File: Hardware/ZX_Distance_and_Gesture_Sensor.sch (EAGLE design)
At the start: 27 parts, among them Q1 MMBT2222A, Q2 MOSFET-NCHANNEL2N7002PW

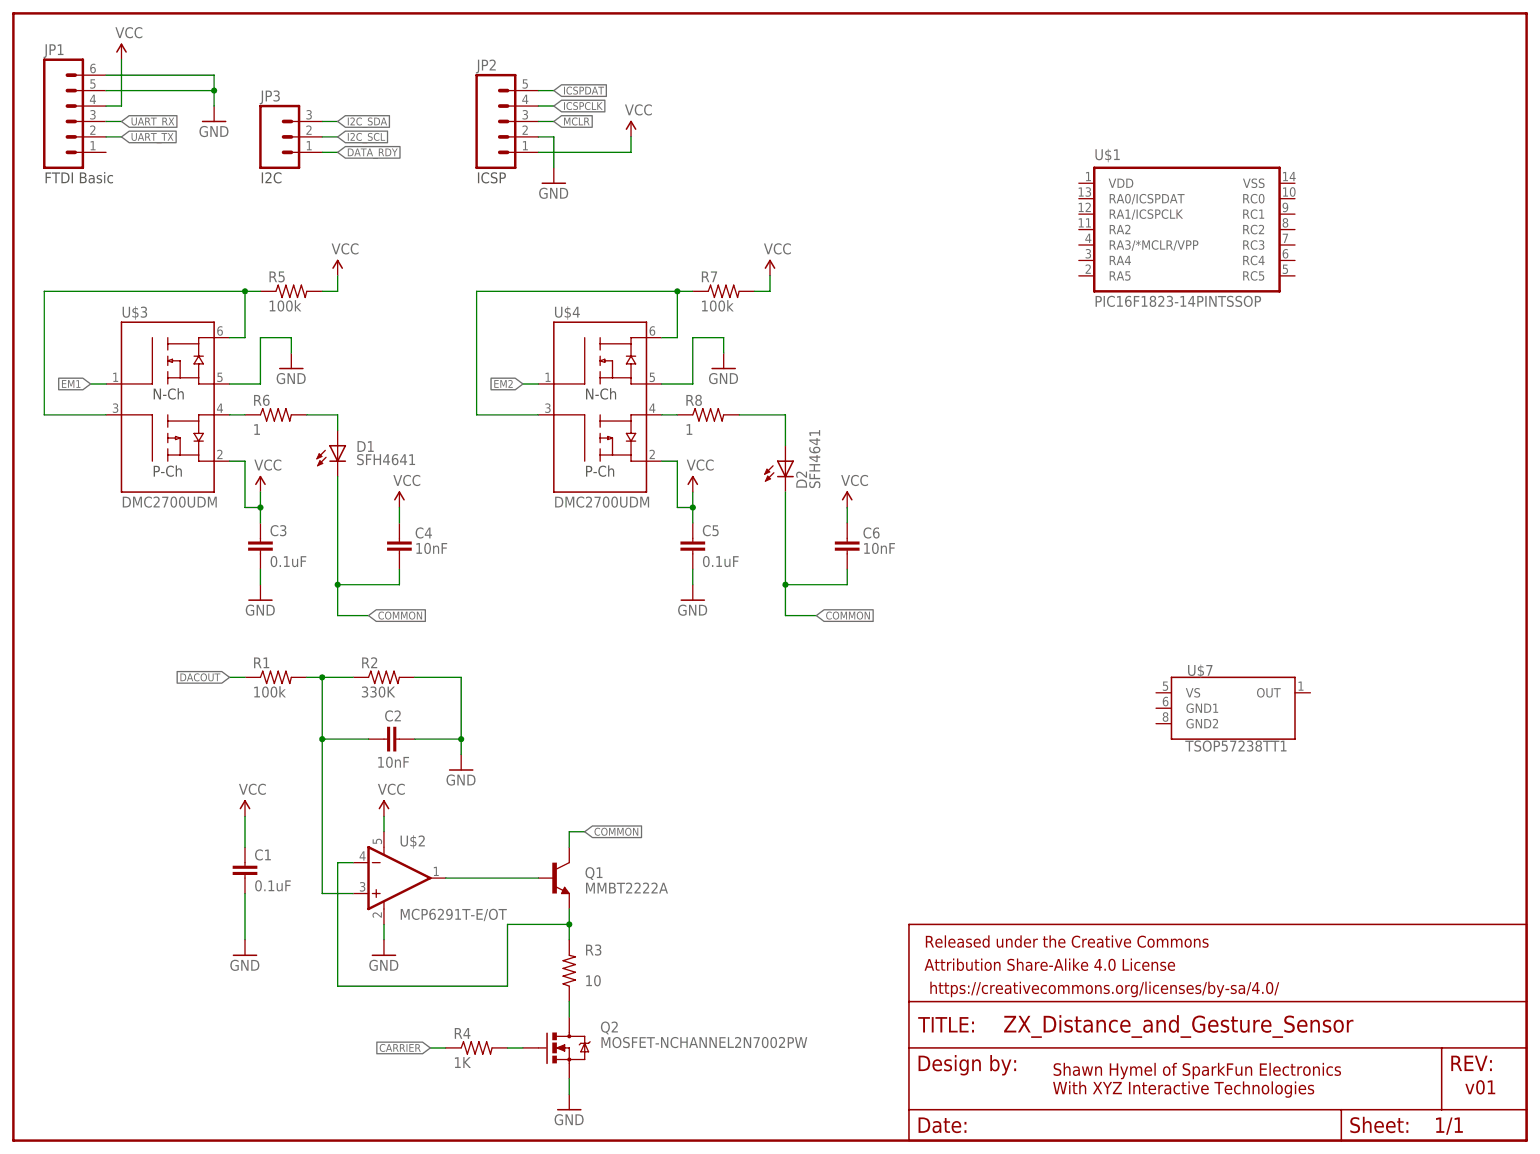
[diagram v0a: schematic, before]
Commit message: Created initial schematic
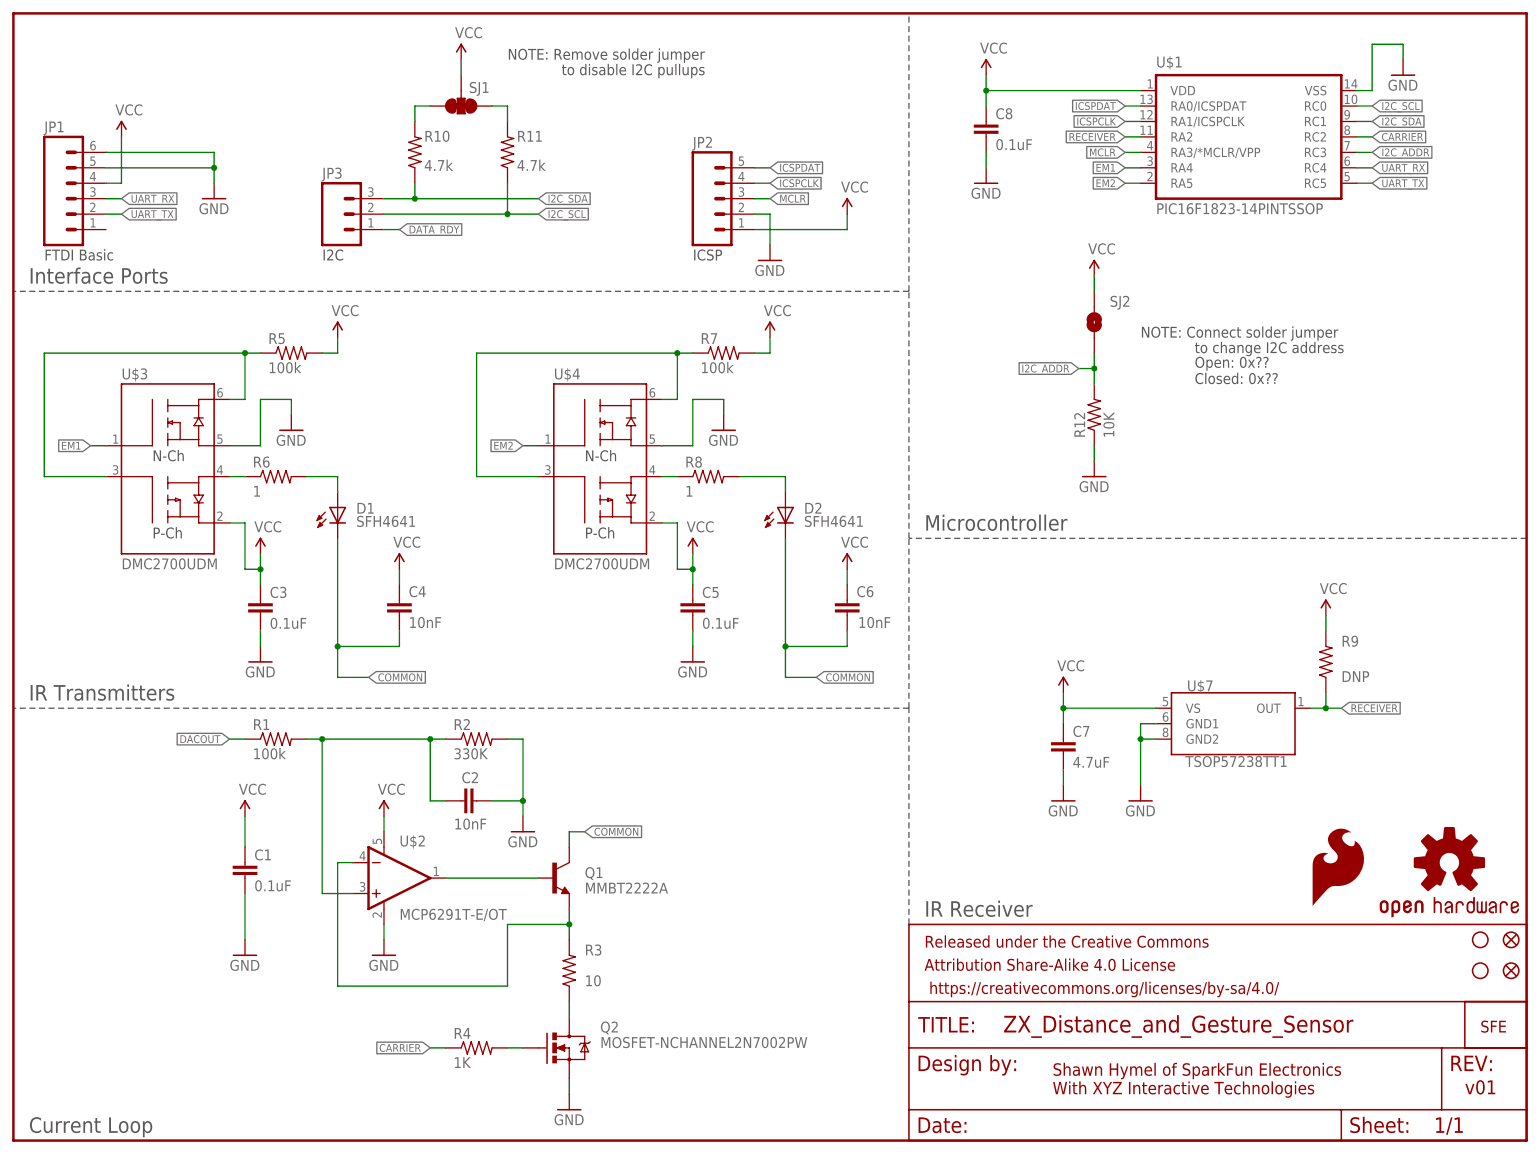
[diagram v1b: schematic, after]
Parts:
- added C7: 4.7uF, SparkFun-Capacitors:4.7UF-6.3V-10%(0603)0603
- added C8: 0.1uF, SparkFun-Capacitors:0.1UF-25V(+80/-20%)(0603)
- added FID1, FID2: FIDUCIAL1X2, SparkFun-Aesthetics:FIDUCIAL1X2
- added LOGO1: SFE_LOGO_FLAME.1_INCH, SparkFun-Aesthetics:SFE_LOGO_FLAME.1_INCH
- added LOGO2: OSHW-LOGOS, SparkFun-Aesthetics:OSHW-LOGOS
- added R10, R11: 4.7k, SparkFun-Resistors:4.7KOHM1/10W1%(0603)
- added R12: 10K, SparkFun-Resistors:10KOHM1/10W1%(0603)0603
- added R9: DNP, SparkFun-Resistors:RESISTOR0603
- added SJ1: (no value), SparkFun-Passives:SOLDERJUMPER_2WAYPASTE1&2&3
- added SJ2: SOLDERJUMPERNO, SparkFun-Passives:SOLDERJUMPERNO
- added STANDOFF1, STANDOFF2: STAND-OFF, SparkFun-Electromechanical:STAND-OFF
- added U$5: SFE_LOGO_NAME_WEB, SparkFun-Aesthetics:SFE_LOGO_NAME_WEB
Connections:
- new net I2C_ADDR: R12.2, SJ2.1, U$1.RC3
- new net N$10: R10.2, SJ1.3
- new net N$13: R11.2, SJ1.1
- new net RECEIVER: R9.1, U$1.RA2, U$7.OUT
- net CARRIER: now also U$1.RC2
- net EM1: now also U$1.RA4
- net EM2: now also U$1.RA5
- net GND: now also C7.2, C8.2, R12.1, U$1.VSS, U$7.GND1, U$7.GND2
- net I2C_SCL: now also R11.1, U$1.RC0
- net I2C_SDA: now also R10.1, U$1.RC1
- net ICSPCLK: now also U$1.RA1/ICSPCLK
- net ICSPDAT: now also U$1.RA0/ICSPDAT
- net MCLR: now also U$1.RA3/*MCLR/VPP
- net UART_RX: now also U$1.RC4
- net UART_TX: now also U$1.RC5
- net VCC: now also C7.1, C8.1, R9.2, SJ1.2, SJ2.2, U$1.VDD, U$7.VS
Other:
- note added: "Current Loop"
- note added: "IR Receiver"
- note added: "IR Transmitters"
- note added: "Interface Ports"
- note added: "Microcontroller"
- note added: "NOTE: Connect solder jumper"
- note added: "NOTE: Remove solder jumper"
- note added: "Open: 0x?? Closed: 0x??"
- note added: "to change I2C address"
- note added: "to disable I2C pullups"
- moved on the sheet: C2, C3, C4, C5, C6, D1, D2, JP1, JP2, JP3, R1, R2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

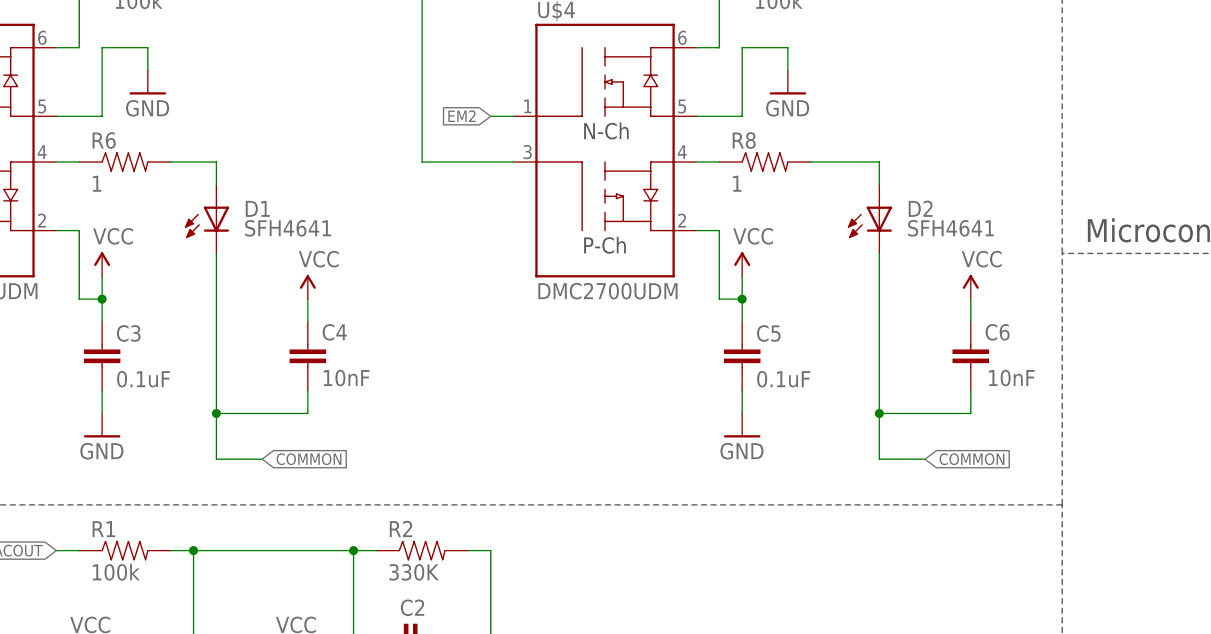
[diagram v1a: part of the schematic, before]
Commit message: Placed components on PCB and started layout
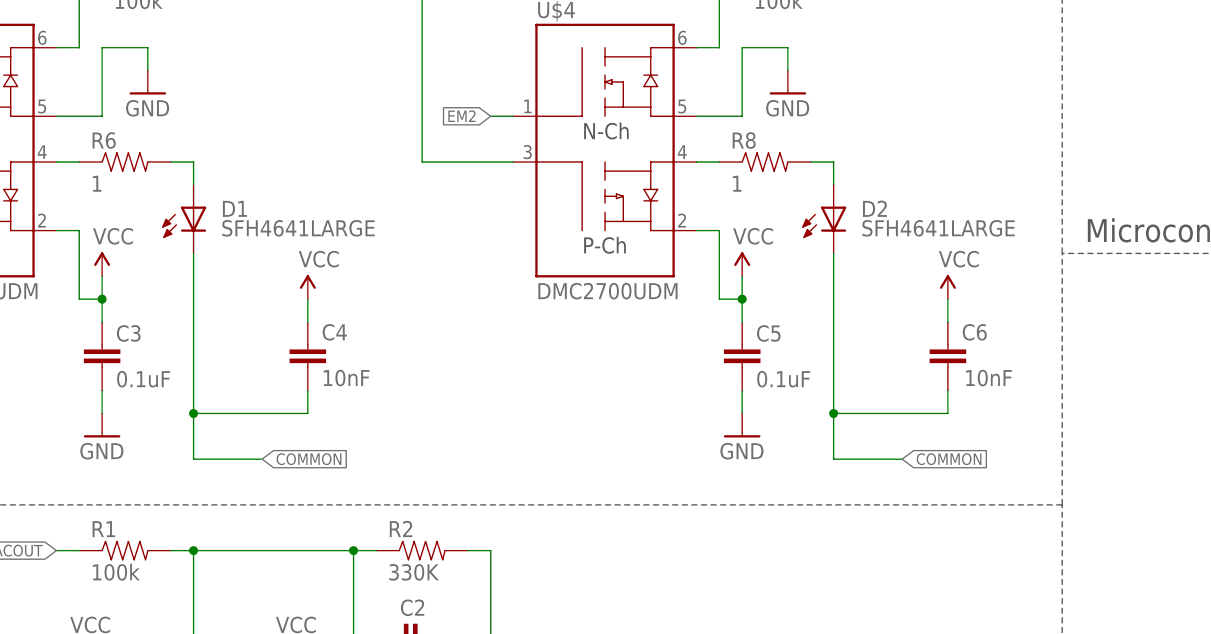
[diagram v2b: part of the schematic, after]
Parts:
- D1, D2: value SFH4641 -> SFH4641LARGE; device SparkFun-LED:SFH4641 -> SparkFun-LED:SFH4641LARGE
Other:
- moved on the sheet: C6, D1, D2
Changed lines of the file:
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@@
 <part name="GND5" library="SparkFun-Aesthetics" deviceset="GND" device=""/>
 <part name="GND6" library="SparkFun-Aesthetics" deviceset="GND" device=""/>
-<part name="D1" library="SparkFun-LED" deviceset="SFH4641" device=""/>
+<part name="D1" library="SparkFun-LED" deviceset="SFH4641" device="LARGE" value="SFH4641LARGE"/>
 <part name="R5" library="SparkFun-Resistors" deviceset="100KOHM1/10W1%(0603)" device="" value="100k"/>
 <part name="R6" library="SparkFun-Resistors" deviceset="1OHM1/10W1%(0603)" device="" value="1"/>
@@
 <part name="GND11" library="SparkFun-Aesthetics" deviceset="GND" device=""/>
 <part name="SUPPLY11" library="SparkFun-Aesthetics" deviceset="VCC" device=""/>
-<part name="D2" library="SparkFun-LED" deviceset="SFH4641" device=""/>
+<part name="D2" library="SparkFun-LED" deviceset="SFH4641" device="LARGE" value="SFH4641LARGE"/>
 <part name="SUPPLY12" library="SparkFun-Aesthetics" deviceset="VCC" device=""/>
 <part name="GND12" library="SparkFun-Aesthetics" deviceset="GND" device=""/>
@@
 <instance part="GND5" gate="1" x="38.1" y="30.48"/>
 <instance part="GND6" gate="1" x="91.44" y="5.08"/>
-<instance part="D1" gate="G$1" x="53.34" y="104.14" smashed="yes">
-<attribute name="NAME" x="56.388" y="103.124" size="1.778" layer="95"/>
-<attribute name="VALUE" x="56.388" y="100.965" size="1.778" layer="96"/>
+<instance part="D1" gate="G$1" x="50.8" y="104.14" smashed="yes">
+<attribute name="NAME" x="53.848" y="103.124" size="1.778" layer="95"/>
+<attribute name="VALUE" x="53.848" y="100.965" size="1.778" layer="96"/>
 </instance>
 <instance part="R5" gate="G$1" x="45.72" y="129.54"/>
@@
 <attribute name="VALUE" x="113.284" y="84.201" size="1.778" layer="96"/>
 </instance>
-<instance part="C6" gate="G$1" x="137.16" y="88.9" smashed="yes" rot="R180">
-<attribute name="NAME" x="138.684" y="89.408" size="1.778" layer="95"/>
-<attribute name="VALUE" x="138.938" y="84.328" size="1.778" layer="96"/>
-</instance>
-<instance part="SUPPLY9" gate="G$1" x="137.16" y="93.98"/>
+<instance part="C6" gate="G$1" x="134.62" y="88.9" smashed="yes" rot="R180">
+<attribute name="NAME" x="136.144" y="89.408" size="1.778" layer="95"/>
+<attribute name="VALUE" x="136.398" y="84.328" size="1.778" layer="96"/>
+</instance>
+<instance part="SUPPLY9" gate="G$1" x="134.62" y="93.98"/>
 <instance part="SUPPLY10" gate="G$1" x="111.76" y="96.52"/>
 <instance part="GND10" gate="1" x="111.76" y="78.74"/>
@@
 <instance part="GND11" gate="1" x="185.42" y="55.88"/>
 <instance part="SUPPLY11" gate="G$1" x="172.72" y="73.66"/>
-<instance part="D2" gate="G$1" x="127" y="104.14" smashed="yes">
-<attribute name="NAME" x="130.048" y="103.124" size="1.778" layer="95"/>
-<attribute name="VALUE" x="130.048" y="100.965" size="1.778" layer="96"/>
+<instance part="D2" gate="G$1" x="121.92" y="104.14" smashed="yes">
+<attribute name="NAME" x="124.968" y="103.124" size="1.778" layer="95"/>
+<attribute name="VALUE" x="124.968" y="100.965" size="1.778" layer="96"/>
 </instance>
 <instance part="SUPPLY12" gate="G$1" x="215.9" y="86.36"/>
@@
 <pinref part="C6" gate="G$1" pin="2"/>
 <pinref part="SUPPLY9" gate="G$1" pin="VCC"/>
-<wire x1="137.16" y1="91.44" x2="137.16" y2="93.98" width="0.1524" layer="91"/>
+<wire x1="134.62" y1="91.44" x2="134.62" y2="93.98" width="0.1524" layer="91"/>
 </segment>
 <segment>
@@
 <segment>
 <pinref part="D1" gate="G$1" pin="C"/>
-<wire x1="53.34" y1="99.06" x2="53.34" y2="81.28" width="0.1524" layer="91"/>
-<wire x1="53.34" y1="81.28" x2="53.34" y2="76.2" width="0.1524" layer="91"/>
-<wire x1="53.34" y1="76.2" x2="58.42" y2="76.2" width="0.1524" layer="91"/>
+<wire x1="50.8" y1="99.06" x2="50.8" y2="81.28" width="0.1524" layer="91"/>
+<wire x1="50.8" y1="81.28" x2="50.8" y2="76.2" width="0.1524" layer="91"/>
+<wire x1="50.8" y1="76.2" x2="58.42" y2="76.2" width="0.1524" layer="91"/>
 <label x="58.42" y="76.2" size="1.27" layer="95" xref="yes"/>
 <pinref part="C4" gate="G$1" pin="1"/>
 <wire x1="63.5" y1="83.82" x2="63.5" y2="81.28" width="0.1524" layer="91"/>
-<wire x1="63.5" y1="81.28" x2="53.34" y2="81.28" width="0.1524" layer="91"/>
-<junction x="53.34" y="81.28"/>
-</segment>
-<segment>
-<wire x1="127" y1="99.06" x2="127" y2="81.28" width="0.1524" layer="91"/>
-<wire x1="127" y1="81.28" x2="127" y2="76.2" width="0.1524" layer="91"/>
-<wire x1="127" y1="76.2" x2="132.08" y2="76.2" width="0.1524" layer="91"/>
+<wire x1="63.5" y1="81.28" x2="50.8" y2="81.28" width="0.1524" layer="91"/>
+<junction x="50.8" y="81.28"/>
+</segment>
+<segment>
+<wire x1="121.92" y1="99.06" x2="121.92" y2="81.28" width="0.1524" layer="91"/>
+<wire x1="121.92" y1="81.28" x2="121.92" y2="76.2" width="0.1524" layer="91"/>
+<wire x1="121.92" y1="76.2" x2="129.54" y2="76.2" width="0.1524" layer="91"/>
 <pinref part="C6" gate="G$1" pin="1"/>
-<wire x1="137.16" y1="83.82" x2="137.16" y2="81.28" width="0.1524" layer="91"/>
-<wire x1="137.16" y1="81.28" x2="127" y2="81.28" width="0.1524" layer="91"/>
-<junction x="127" y="81.28"/>
-<label x="132.08" y="76.2" size="1.27" layer="95" xref="yes"/>
+<wire x1="134.62" y1="83.82" x2="134.62" y2="81.28" width="0.1524" layer="91"/>
+<wire x1="134.62" y1="81.28" x2="121.92" y2="81.28" width="0.1524" layer="91"/>
+<junction x="121.92" y="81.28"/>
+<label x="129.54" y="76.2" size="1.27" layer="95" xref="yes"/>
 <pinref part="D2" gate="G$1" pin="C"/>
 </segment>
@@
 <pinref part="R6" gate="G$1" pin="2"/>
 <pinref part="D1" gate="G$1" pin="A"/>
-<wire x1="48.26" y1="109.22" x2="53.34" y2="109.22" width="0.1524" layer="91"/>
-<wire x1="53.34" y1="109.22" x2="53.34" y2="106.68" width="0.1524" layer="91"/>
+<wire x1="48.26" y1="109.22" x2="50.8" y2="109.22" width="0.1524" layer="91"/>
+<wire x1="50.8" y1="109.22" x2="50.8" y2="106.68" width="0.1524" layer="91"/>
 </segment>
 </net>
@@
 <segment>
 <pinref part="R8" gate="G$1" pin="2"/>
-<wire x1="119.38" y1="109.22" x2="127" y2="109.22" width="0.1524" layer="91"/>
-<wire x1="127" y1="109.22" x2="127" y2="106.68" width="0.1524" layer="91"/>
+<wire x1="119.38" y1="109.22" x2="121.92" y2="109.22" width="0.1524" layer="91"/>
+<wire x1="121.92" y1="109.22" x2="121.92" y2="106.68" width="0.1524" layer="91"/>
 <pinref part="D2" gate="G$1" pin="A"/>
 </segment>

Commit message: More progress on layout
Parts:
- D1, D2: value SFH4641LARGE -> SFH4641OVERSIZE; device SparkFun-LED:SFH4641LARGE -> SparkFun-LED:SFH4641OVERSIZE
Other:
- moved on the sheet: C5, C6, D2, R7, R8, U$4
